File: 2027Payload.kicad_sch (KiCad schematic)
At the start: 57 parts, among them J1 USB_C_Receptacle_USB2.0_16P, J10 Conn_02x03_Odd_Even, J11 Conn_01x03, J2 Conn_01x01, J3 Conn_01x03, J4 Conn_01x03, J5 Conn_01x03, J6 Conn_01x04, J7 Conn_01x04, J8 Conn_01x04, J9 Conn_01x01, SW1 SW_Push, SW2 SW_Push, U1 ESP32-S3-WROOM-1-N8R8, U3 TPS22965DSGT, U6 USBLC6-2SC6, U7 TLV75533PDBVR, U9 TPS2113ADRBR

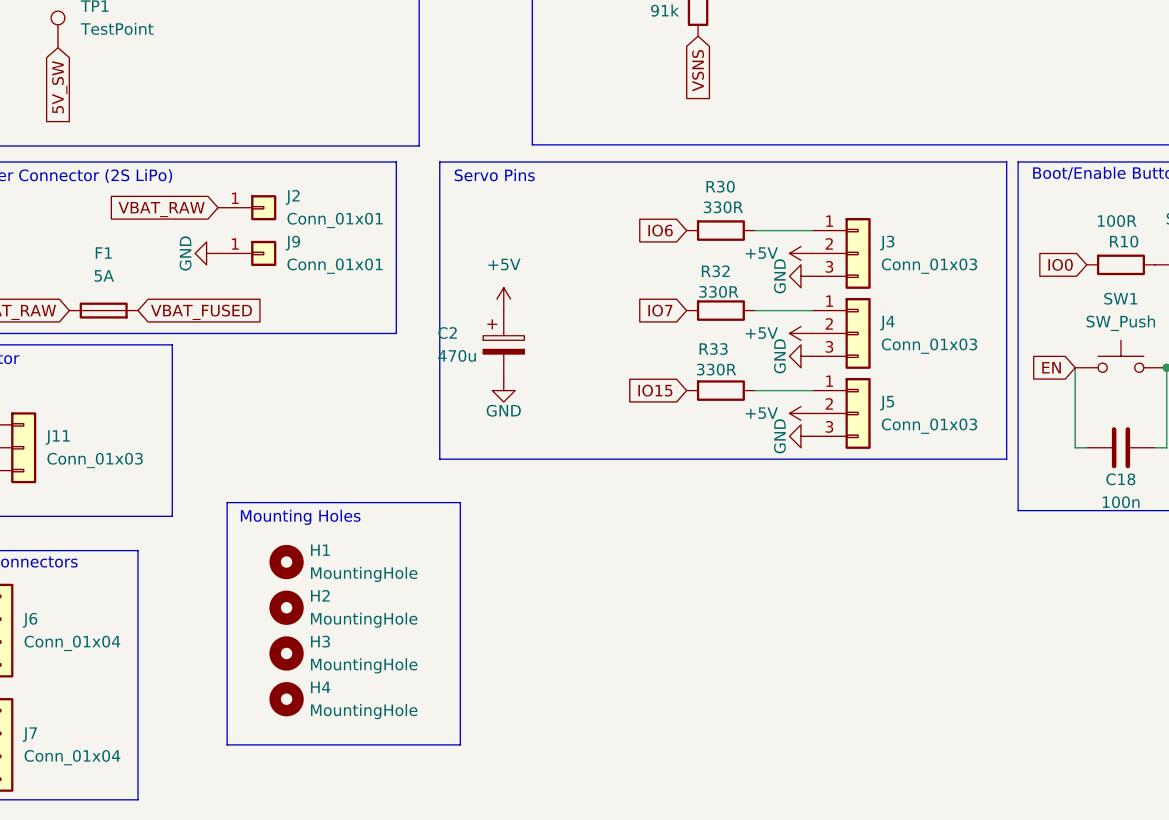
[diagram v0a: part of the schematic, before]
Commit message: Added pins for one extra servo.
5V, GND, IO14
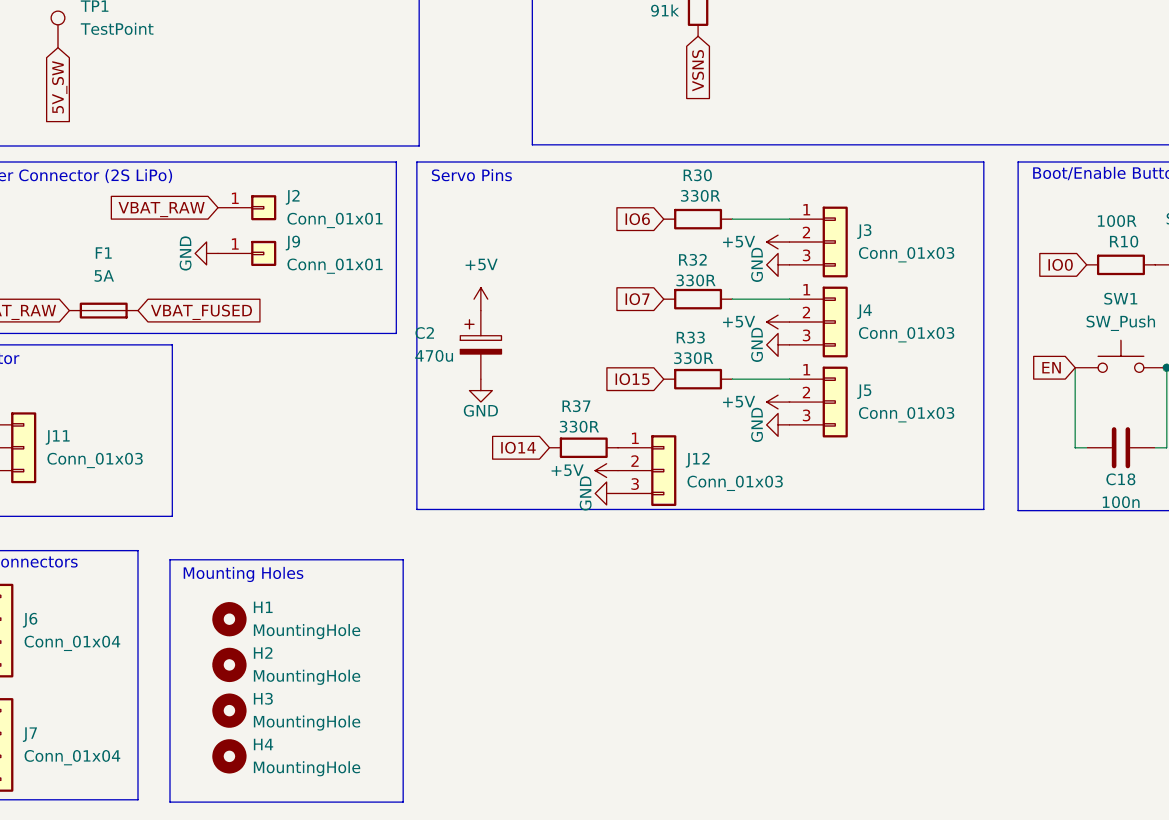
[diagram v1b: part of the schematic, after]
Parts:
- added J12: Conn_01x03, Connector_PinHeader_2.54mm:PinHeader_1x03_P2.54mm_Vertical, symbol Connector_Generic:Conn_01x03
- added R37: 330R, Capacitor_SMD:C_0603_1608Metric, symbol Device:R
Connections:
- net +5V: now also J12.2 (Pin_2)
- net GND: now also J12.3 (Pin_3)
- net IO14: now also R37.2
- new net: J12.1 (Pin_1), R37.1
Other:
- moved on the sheet: C2, H1, H2, H3, H4, J3, J4, J5, R30, R32, R33

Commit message: Updated BOM
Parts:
- F1: Distributor Link (none) -> https://www.digikey.com/en/products/detail/littelfuse-inc/0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; Manufacturer Part Number (none) -> 0448005.MR
- U3: Distributor Link (none) -> https://www.digikey.com/en/products/detail/texas-instrument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; Manufacturer Part Number (none) -> TPS22965DSGT
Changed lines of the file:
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@@
 			)
 		)
-		(property "Distributor Link" ""
+		(property "Distributor Link" "https://www.digikey.com/en/products/detail/littelfuse-inc/0448005-MR/1211090"
 			(at 130.81 143.51 90)
 			(hide yes)
@@
 			)
 		)
-		(property "Manufacturer Part Number" ""
+		(property "Manufacturer Part Number" "0448005.MR"
 			(at 130.81 143.51 90)
 			(hide yes)
@@
 			)
 		)
+		(property "Distributor Link" "https://www.digikey.com/en/products/detail/texas-instruments/TPS22965DSGT/3661875?s=N4IgTCBcDaICoAUDKYwE4BsBWAIkg4nCALoC%2BQA"
+			(at 229.87 41.91 0)
+			(hide yes)
+			(show_name no)
+			(do_not_autoplace no)
+			(effects
+				(font
+					(size 1.27 1.27)
+				)
+			)
+		)
+		(property "Manufacturer Part Number" "TPS22965DSGT"
+			(at 229.87 41.91 0)
+			(hide yes)
+			(show_name no)
+			(do_not_autoplace no)
+			(effects
+				(font
+					(size 1.27 1.27)
+				)
+			)
+		)

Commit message: Final BOM
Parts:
- C12, C13, C15, C16, C17: Distributor Link (none) -> https://www.digikey.com/en/products/detail/taiyo-yuden/UMK1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; Manufacturer Part Number (none) -> UMK107AB7105KA-TT
- C14, C29, C5: Distributor Link (none) -> https://www.digikey.com/en/products/detail/murata-electroni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; Manufacturer Part Number (none) -> GRM188R61E106MA73D
- C18, C22, C23, C42, C43, C45: Distributor Link (none) -> https://www.digikey.com/en/products/detail/kemet/C0603C104K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; Manufacturer Part Number (none) -> C0603C104K5RACTU
- C2: Distributor Link (none) -> https://www.digikey.com/en/products/detail/vishay-beyschlag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; Manufacturer Part Number (none) -> MAL215097501E3
- C40, C41, C44: Distributor Link (none) -> https://www.digikey.com/en/products/detail/samsung-electro-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; Manufacturer Part Number (none) -> CL10A226MO7JZNC
- C46: Distributor Link (none) -> https://www.digikey.com/en/products/detail/kemet/C0603C103K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; Manufacturer Part Number (none) -> C0603C103K5RACTU
- D1: Distributor Link (none) -> https://www.digikey.com/en/products/detail/w-rth-elektronik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; Manufacturer Part Number (none) -> 150080RS75000
- J10: Distributor Link (none) -> https://www.digikey.com/en/products/detail/sullins-connecto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; Manufacturer Part Number (none) -> PRPC003DAAN-RC
- J11: Distributor Link (none) -> https://www.digikey.com/en/products/detail/jst-sales-americ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; Manufacturer Part Number (none) -> B3B-PH-SM4-TBT
- J12, J3, J4, J5: Distributor Link (none) -> https://www.digikey.com/en/products/detail/harwin-inc/M20-9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; Manufacturer Part Number (none) -> M20-9990345
- J2, J9, TP1: now left out of the parts list
- J8: Distributor Link (none) -> https://www.adafruit.com/product/4392; Manufacturer Part Number (none) -> 2mm 4-pin Horizontal Connector - JST PH Compatible - 10 Pac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
- R10: footprint Capacitor_SMD:C_0603_1608Metric -> Resistor_SMD:R_0603_1608Metric; Distributor Link (none) -> https://www.digikey.com/en/products/detail/yageo/RC0603FR-0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; Manufacturer Part Number (none) -> RC0603FR-07100RL
- R15: footprint Capacitor_SMD:C_0603_1608Metric -> Resistor_SMD:R_0603_1608Metric; Distributor Link (none) -> https://www.digikey.com/en/products/detail/bourns-inc/CR060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; Manufacturer Part Number (none) -> CR0603-FX-3320ELF
- R16: footprint Capacitor_SMD:C_0603_1608Metric -> Resistor_SMD:R_0603_1608Metric; Distributor Link (none) -> https://www.digikey.com/en/products/detail/yageo/RC0603JR-0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; Manufacturer Part Number (none) -> RC0603JR-0791KL
- R22, R36: footprint Capacitor_SMD:C_0603_1608Metric -> Resistor_SMD:R_0603_1608Metric; Distributor Link (none) -> https://www.digikey.com/en/products/detail/yageo/RC0603FR-0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; Manufacturer Part Number (none) -> RC0603FR-07100KL
- R23: footprint Capacitor_SMD:C_0603_1608Metric -> Resistor_SMD:R_0603_1608Metric; Distributor Link (none) -> https://www.digikey.com/en/products/detail/yageo/RC0603JR-0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; Manufacturer Part Number (none) -> RC0603JR-0743KL
- R30, R32, R33, R37: footprint Capacitor_SMD:C_0603_1608Metric -> Resistor_SMD:R_0603_1608Metric; Distributor Link (none) -> https://www.digikey.com/en/products/detail/yageo/RC0603FR-0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; Manufacturer Part Number (none) -> RC0603FR-07330RL
- R31: footprint Capacitor_SMD:C_0603_1608Metric -> Resistor_SMD:R_0603_1608Metric; Distributor Link (none) -> https://www.digikey.com/en/products/detail/panasonic-indust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; Manufacturer Part Number (none) -> ERJ-3GEYJ301V
- R7, R8: footprint Capacitor_SMD:C_0603_1608Metric -> Resistor_SMD:R_0603_1608Metric; Distributor Link (none) -> https://www.digikey.com/en/products/detail/yageo/AC0603FR-1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; Manufacturer Part Number (none) -> AC0603FR-135K1L
- R9: footprint Capacitor_SMD:C_0603_1608Metric -> Resistor_SMD:R_0603_1608Metric; Distributor Link (none) -> https://www.digikey.com/en/products/detail/yageo/RC0603JR-0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; Manufacturer Part Number (none) -> RC0603JR-0710KL

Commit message: Final BOM v2
TI TPS543620RPYR not in stock at DigiKey; abundant stock at Mouser, so updated BOM accordingly
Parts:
- C12, C13, C15, C16, C17: Manufacturer Part Number UMK107AB7105KA-TT -> UMK107AB7105KA-T
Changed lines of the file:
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@@
 			)
 		)
-		(property "Manufacturer Part Number" "UMK107AB7105KA-TT"
+		(property "Manufacturer Part Number" "UMK107AB7105KA-T"
 			(at 271.78 149.86 0)
 			(hide yes)
@@
 			)
 		)
-		(property "Manufacturer Part Number" "UMK107AB7105KA-TT"
+		(property "Manufacturer Part Number" "UMK107AB7105KA-T"
 			(at 194.31 88.9 90)
 			(hide yes)
@@
 			)
 		)
-		(property "Manufacturer Part Number" "UMK107AB7105KA-TT"
+		(property "Manufacturer Part Number" "UMK107AB7105KA-T"
 			(at 194.31 83.82 90)
 			(hide yes)
@@
 			)
 		)
-		(property "Manufacturer Part Number" "UMK107AB7105KA-TT"
+		(property "Manufacturer Part Number" "UMK107AB7105KA-T"
 			(at 83.82 180.34 0)
 			(hide yes)
@@
 			)
 		)
-		(property "Manufacturer Part Number" "UMK107AB7105KA-TT"
+		(property "Manufacturer Part Number" "UMK107AB7105KA-T"
 			(at 30.48 184.15 0)
 			(hide yes)
